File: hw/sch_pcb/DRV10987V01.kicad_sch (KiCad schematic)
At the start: 22 parts, among them IC1 DRV10975PWPR, J1 Umin ... Umax, J2 HEADER_2x05_PARALLEL, J3 HEADER_2x04_PARALLEL, J4 HEADER_2x02_PARALLEL, M1 HOLE M3, M2 HOLE M3, M3 HOLE, M4 HOLE

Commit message: schematics and layout improvements
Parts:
- removed J4: HEADER_2x02_PARALLEL, symbol MLAB_HEADER:HEADER_2x02_PARALLEL
- removed NT1: NetTie_2, symbol Device:NetTie_2
- added J11: WAGO, TerminalBlock_WAGO:TerminalBlock_WAGO_236-102_1x02_P5.00mm_45Degree, symbol MLAB_HEADER:HEADER_1x02
- added J12: WAGO, TerminalBlock_WAGO:TerminalBlock_WAGO_236-103_1x03_P5.00mm_45Degree, symbol MLAB_HEADER:HEADER_1x03
- added J4: JUMPER, Mlab_Pin_Headers:Straight_1x02, symbol MLAB_HEADER:HEADER_2x01
- added J5: AUX, Mlab_Pin_Headers:Straight_2x03, symbol header:HEADER_2x03_PARALLEL
- added J6: MOTOR, Mlab_Pin_Headers:Straight_2x03, symbol MLAB_HEADER:HEADER_2x03_PARALLEL
- added L1: 47uH DE0703-47, Inductor_SMD:L_Ferrocore_DLG-0703, symbol Device:L
- added R4, R5: 4k7, Resistor_SMD:R_0805_2012Metric, symbol Device:R_Small
- C1: renamed from C8; footprint (none) -> Capacitor_SMD:C_0805_2012Metric; UST_ID (none) -> 5c70984712875079b91f8b53
- C2: renamed from C4; footprint (none) -> Capacitor_SMD:C_0805_2012Metric; UST_ID (none) -> 5c70984712875079b91f8b4c
- C3: footprint (none) -> Capacitor_SMD:C_0805_2012Metric; UST_ID (none) -> 5c70984712875079b91f8b4c
- C4: renamed from C5; footprint (none) -> Capacitor_SMD:C_0805_2012Metric; UST_ID (none) -> 5c70984712875079b91f8b50
- C5: renamed from C6; footprint (none) -> Capacitor_SMD:C_0805_2012Metric; UST_ID (none) -> 5c70984712875079b91f8b50
- C6: renamed from C7; footprint (none) -> Capacitor_SMD:C_0805_2012Metric; UST_ID (none) -> 5c70984712875079b91f8b53
- C7: renamed from C1; UST_ID 5c70984812875079b91f8bbe -> 5c70984712875079b91f8b53
- C8: renamed from C2; UST_ID 5c70984812875079b91f8bf2 -> 5c70984712875079b91f8b4c; UST_id C0805_100n -> (none)
- IC1: value DRV10975PWPR -> DRV10987DPWPR; footprint SOP65P640X120-25N -> Mlab_IO:TSSOP-24_4.4x7.8mm_P0.65mm_PowerPAD; Manufacturer_Part_Number DRV10975PWPR -> DRV10987DPWPR; Mouser Part Number 595-DRV10975PWPR -> 595-DRV10987DPWPR; UST_ID (none) -> 649ebe2a76c82a1d3b578220
- J10: renamed from J1; value Umin ... Umax -> PWR
- J2: value HEADER_2x05_PARALLEL -> I2C; footprint (none) -> Mlab_Pin_Headers:Straight_2x05
- J3: footprint (none) -> Mlab_Pin_Headers:Straight_2x04
- M3, M4: value HOLE -> HOLE M3
- R1: renamed from R2; value 4k5 -> 4k7; footprint (none) -> Resistor_SMD:R_0805_2012Metric; UST_ID (none) -> 5c70984612875079b91f8995
- R2: renamed from R1; value 4k5 -> 4k7; footprint (none) -> Resistor_SMD:R_0805_2012Metric; UST_ID (none) -> 5c70984612875079b91f8995
- R3: value 4k5 -> 4k7; footprint (none) -> Resistor_SMD:R_0805_2012Metric; UST_ID (none) -> 5c70984612875079b91f8995
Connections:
- net GNDPWR is gone; now on net GND: IC1.15 (PGND_1), IC1.16 (PGND_2), IC1.25 (GND_2)
- net VREF is gone; now on net GND: J3.7, J3.8
- net +12V: now also C6.2, J3.3, J3.4, J3.5, J3.6, J11.2
- net DIR: now also J5.1, J5.2, R4.2; no longer J3.3, J3.4
- net FG: now also J5.5, J5.6; no longer J3.5, J3.6
- net GND: now also J2.1, J2.10, J2.2, J2.9, J3.1, J3.2, J11.1
- net STEP: now also J5.3, J5.4, R5.2; no longer J3.1, J3.2
- net U: now also J12.3, J6.1, J6.2
- net V: now also J12.2, J6.3, J6.4
- net W: now also J12.1, J6.5, J6.6
- removed net VCC: C6.2, C7.1, C8.1, D1.1 (K), J10.3, J10.4, J2.5, J2.6, R1.1, R2.1, R3.1
- net VREG renamed +5V
- net +5V: now also C7.1, C8.1, D1.1 (K), J10.3, J10.4, J4.2, L1.1; no longer IC1.4 (SW)
- new net: IC1.4 (SW), L1.2
- new net VDD: J2.5, J2.6, J4.1, R1.1, R2.1, R3.1, R4.1, R5.1
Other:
- note removed: "Adjust power voltage range and symbol"
- note removed: "Generally a load module has mounting holes connected to the ground."
- note removed: "Power source modules has mountig holes floating to avoid ground loops."
- note removed: "check if the mounting holles should be connected to ground or not."
- title: NAME -> DRV10975V01A
- moved on the sheet: C1, R3

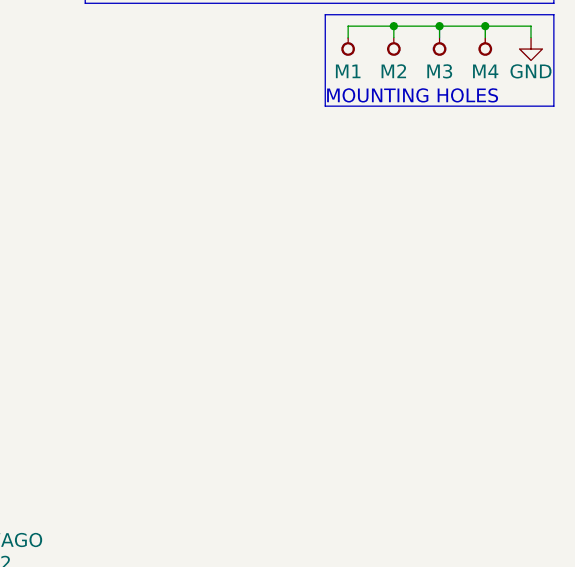
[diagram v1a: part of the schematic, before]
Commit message: update silkscreen, add 5v indicator
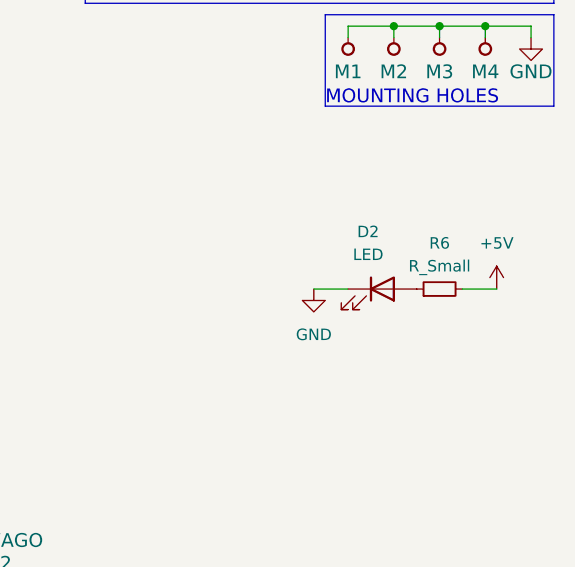
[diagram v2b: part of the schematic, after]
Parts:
- added D2: LED, Mlab_D:LED_1206_2, symbol Device:LED
- added R6: R_Small, Resistor_SMD:R_0805_2012Metric, symbol Device:R_Small
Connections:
- net +5V: now also R6.2
- net GND: now also D2.1 (K)
- new net: D2.2 (A), R6.1
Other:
- title: DRV10975V01A -> DRV10987V01A

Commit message: uprava napajeni 3v3
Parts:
- removed J4: JUMPER, Mlab_Pin_Headers:Straight_1x02, symbol MLAB_HEADER:HEADER_2x01
- added R7: 100R, Resistor_SMD:R_0805_2012Metric, symbol Device:R_Small
- R4, R5: value 4k7 -> DNF
- R6: value R_Small -> R
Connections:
- net VDD: now also R7.1
- net V3P3: now reaches C4.2, IC1.9 (V3P3)
- net V3P3: now also R7.2
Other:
- moved on the sheet: J11, J12, J6

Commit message: Edit PCB and schema
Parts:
- C2: value 100nF -> 10nF; UST_ID 5c70984712875079b91f8b4c -> (none)
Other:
- note added: "POWER OUTPUT 5V max 100mA"
- note removed: "POWER INPUT"
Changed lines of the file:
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@@
     (stroke (width 0) (type default))
   )
-  (text "POWER INPUT" (at 227.33 48.26 0)
+  (text "POWER OUTPUT 5V max 100mA" (at 227.33 48.26 0)
     (effects (font (size 1.524 1.524)) (justify left bottom))
   )
@@
   (symbol (lib_id "Device:L") (at 78.74 77.47 90) (unit 1)
     (in_bom yes) (on_board yes) (dnp no)
-    (property "Reference" "L1" (at 80.01 78.74 90)
-      (effects (font (size 1.27 1.27)))
-    )
-    (property "Value" "47uH DE0703-47" (at 76.2 78.74 90)
+    (property "Reference" "L1" (at 83.185 76.2 90)
+      (effects (font (size 1.27 1.27)))
+    )
+    (property "Value" "47uH DE0703-47" (at 82.55 78.74 90)
       (effects (font (size 1.27 1.27)))
     )
@@
       (effects (font (size 1.27 1.27)))
     )
-    (property "Value" "100nF" (at 76.2 69.85 90)
+    (property "Value" "10nF" (at 76.2 69.85 90)
       (effects (font (size 1.27 1.27)))
     )
@@
       (effects (font (size 1.27 1.27)) hide)
     )
-    (property "UST_ID" "5c70984712875079b91f8b4c" (at 76.2 72.39 0)
-      (effects (font (size 1.27 1.27)) hide)
-    )
+    (property "UST_ID" "" (at 76.2 72.39 0)
+      (effects (font (size 1.27 1.27)) hide)
+    )

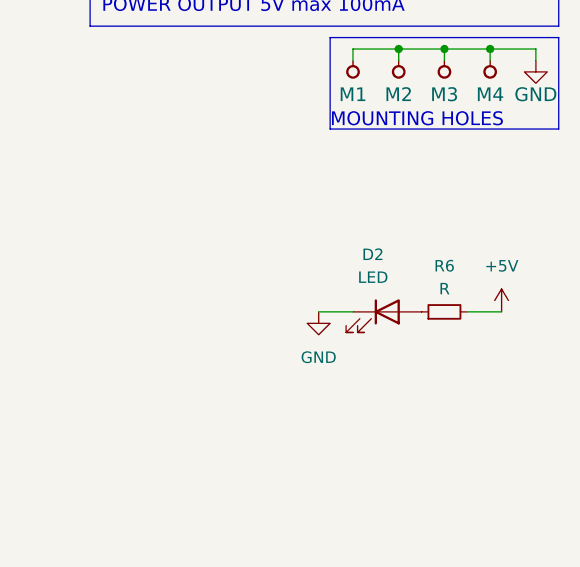
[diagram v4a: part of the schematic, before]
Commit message: Editing component values
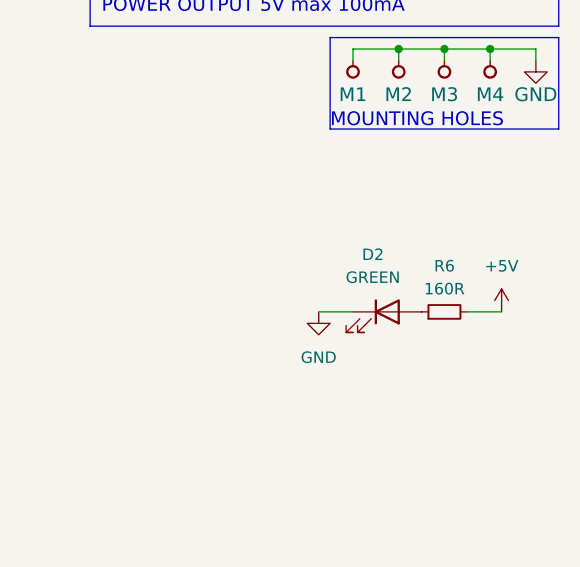
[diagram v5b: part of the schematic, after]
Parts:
- C2: UST_ID (none) -> 5c70984712875079b91f8b49
- D2: value LED -> GREEN; UST_ID (none) -> 5c70984412875079b91f8895
- R6: value R -> 160R; UST_ID (none) -> 5c70984512875079b91f897b
- R7: UST_ID (none) -> 5c70984512875079b91f8977
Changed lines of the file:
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@@
       (effects (font (size 1.27 1.27)))
     )
-    (property "Value" "LED" (at 257.4925 77.47 0)
+    (property "Value" "GREEN" (at 257.4925 77.47 0)
       (effects (font (size 1.27 1.27)))
     )
@@
       (effects (font (size 1.27 1.27)) hide)
     )
+    (property "UST_ID" "5c70984412875079b91f8895" (at 259.08 81.28 0)
+      (effects (font (size 1.27 1.27)) hide)
+    )
     (pin "1")
     (pin "2")
@@
       (effects (font (size 1.27 1.27)) hide)
     )
-    (property "UST_ID" "" (at 76.2 72.39 0)
+    (property "UST_ID" "5c70984712875079b91f8b49" (at 76.2 72.39 0)
       (effects (font (size 1.27 1.27)) hide)
     )
@@
       (effects (font (size 1.27 1.27)) hide)
     )
+    (property "UST_ID" "5c70984512875079b91f8977" (at 115.57 52.07 0)
+      (effects (font (size 1.27 1.27)) hide)
+    )
     (pin "1")
     (pin "2")
@@
       (effects (font (size 1.27 1.27)))
     )
-    (property "Value" "R" (at 265.43 78.74 90)
+    (property "Value" "160R" (at 265.43 78.74 90)
       (effects (font (size 1.27 1.27)))
     )
@@
       (effects (font (size 1.27 1.27)) hide)
     )
+    (property "UST_ID" "5c70984512875079b91f897b" (at 265.43 81.28 0)
+      (effects (font (size 1.27 1.27)) hide)
+    )
